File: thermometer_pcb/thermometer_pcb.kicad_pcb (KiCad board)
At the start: 2 copper layers, 76.6 x 49 mm, 23 parts, among them J1 POWER_IN, J2 TC_IN, J3 EXT_DS1, J4 EXT_DS2, J5 DISP, J6 Conn_01x02, J7 SPI, J8 I2C, J9 ENC, Q1 PN2222A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

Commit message: thermometer_pcb: move to new kicad
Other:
- net class Default removed
- net class PWR removed
- net class tc removed

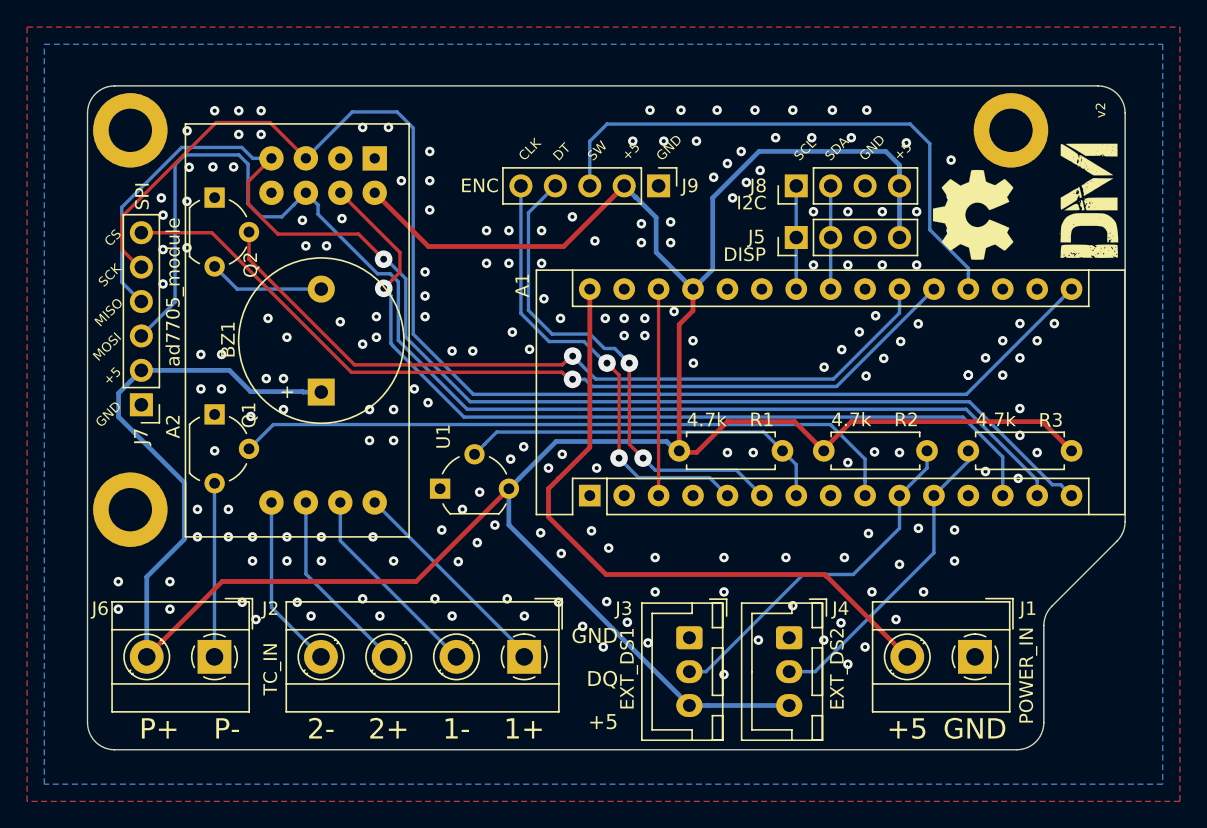
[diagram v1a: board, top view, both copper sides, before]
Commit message: pcb: tune corners radius
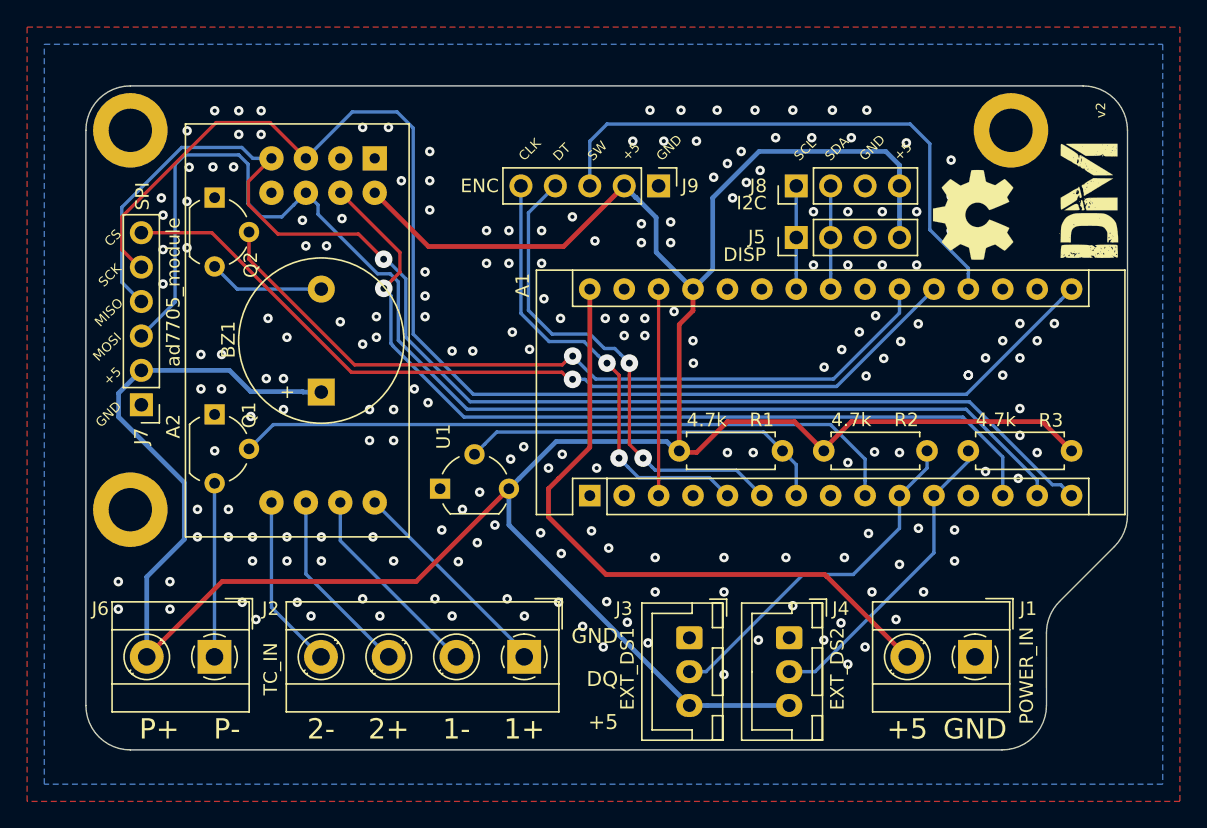
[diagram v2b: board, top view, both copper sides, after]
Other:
- board size 76.6 x 49 mm -> 76.9 x 49 mm
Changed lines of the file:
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@@
   (setup
     (aux_axis_origin 139.446 106.807)
-    (grid_origin 222.205677 44.032604)
+    (grid_origin 148.796676 47.298604)
     (pcbplotparams
       (layerselection 0x030f0_ffffffff)
@@
       (net 1 "GND") (zone_connect 2))
   )
+  (gr_arc (start 219.695641 84.398259) (end 216.415641 84.398259) (angle 45.00852154) (layer "Edge.Cuts") (width 0.1))
+  (gr_arc (start 219.116676 75.698604) (end 222.396676 75.698604) (angle 45) (layer "Edge.Cuts") (width 0.1))
+  (gr_arc (start 219.116676 47.298604) (end 222.396676 47.298604) (angle -90) (layer "Edge.Cuts") (width 0.1))
+  (gr_arc (start 213.136676 89.748604) (end 213.136676 93.028604) (angle -90) (layer "Edge.Cuts") (width 0.1))
+  (gr_arc (start 148.796676 89.748604) (end 145.516676 89.748604) (angle -90) (layer "Edge.Cuts") (width 0.1))
+  (gr_arc (start 148.796676 47.298604) (end 148.796676 44.018604) (angle -90) (layer "Edge.Cuts") (width 0.1))
   (gr_text "v2" (at 220.427677 45.810604 90) (layer "F.SilkS")
     (effects (font (size 0.7 0.7) (thickness 0.1)))
@@
   (gr_circle (center 218.268677 59.018604) (end 218.268677 58.618605) (layer "Dwgs.User") (width 0.1))
   (gr_circle (center 218.268677 74.258604) (end 218.268677 73.858604) (layer "Dwgs.User") (width 0.1))
-  (gr_line (start 145.636676 46.018604) (end 145.636676 91.018604) (layer "Edge.Cuts") (width 0.1))
-  (gr_line (start 216.807463 82.432818) (end 221.63589 77.604391) (layer "Edge.Cuts") (width 0.1))
-  (gr_arc (start 218.221676 83.847031) (end 216.807463 82.432818) (angle -45) (layer "Edge.Cuts") (width 0.1))
-  (gr_line (start 220.221676 44.018604) (end 147.636676 44.018604) (layer "Edge.Cuts") (width 0.1))
-  (gr_arc (start 147.636676 46.018604) (end 147.636676 44.018604) (angle -90) (layer "Edge.Cuts") (width 0.1))
-  (gr_arc (start 147.636676 91.018604) (end 145.636676 91.018604) (angle -90) (layer "Edge.Cuts") (width 0.1))
-  (gr_line (start 147.636676 93.018604) (end 214.221676 93.018604) (layer "Edge.Cuts") (width 0.1))
-  (gr_arc (start 214.221676 91.018604) (end 214.221676 93.018604) (angle -90) (layer "Edge.Cuts") (width 0.1))
-  (gr_line (start 216.221676 91.018604) (end 216.221676 83.847031) (layer "Edge.Cuts") (width 0.1))
-  (gr_arc (start 220.221676 76.190177) (end 221.63589 77.604391) (angle -45) (layer "Edge.Cuts") (width 0.1))
-  (gr_line (start 222.221676 76.190177) (end 222.221676 46.018604) (layer "Edge.Cuts") (width 0.1))
-  (gr_arc (start 220.221676 46.018604) (end 222.221676 46.018604) (angle -90) (layer "Edge.Cuts") (width 0.1))
+  (gr_line (start 145.516676 47.298604) (end 145.516676 89.748604) (layer "Edge.Cuts") (width 0.1))
+  (gr_line (start 217.376676 82.078604) (end 221.435986 78.017914) (layer "Edge.Cuts") (width 0.1))
+  (gr_line (start 219.116676 44.018604) (end 148.796676 44.018604) (layer "Edge.Cuts") (width 0.1))
+  (gr_line (start 148.796676 93.028604) (end 213.136676 93.028604) (layer "Edge.Cuts") (width 0.1))
+  (gr_line (start 216.416676 89.748604) (end 216.415641 84.398259) (layer "Edge.Cuts") (width 0.1))
+  (gr_line (start 222.396676 75.698604) (end 222.396676 47.298604) (layer "Edge.Cuts") (width 0.1))
   (segment (start 202.155677 80.082604) (end 205.568677 76.669604) (width 0.25) (layer "B.Cu") (net 20))
   (segment (start 205.568677 76.669604) (end 205.568677 74.258604) (width 0.25) (layer "B.Cu") (net 20))

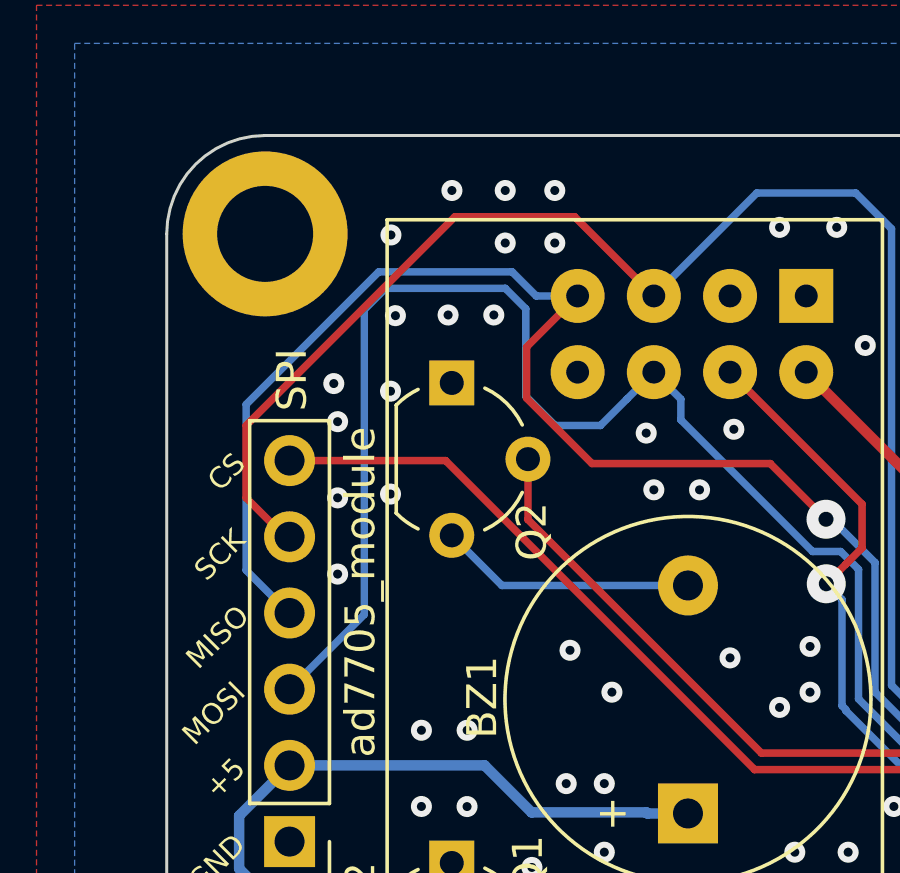
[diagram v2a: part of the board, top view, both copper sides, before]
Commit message: pcb: move some traces
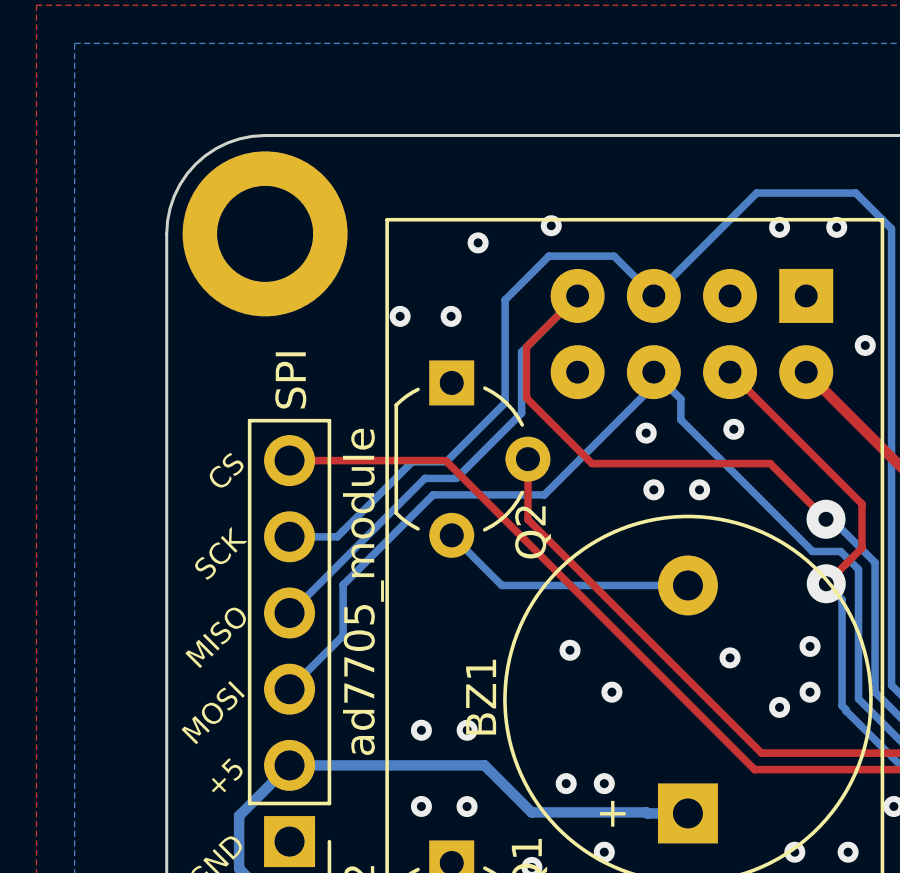
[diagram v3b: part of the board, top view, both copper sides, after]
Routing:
- net /11(**/MOSI): track 95.1 -> 84.9 mm
- net /12(MISO): track 97.1 -> 91.5 mm
- net /13(SCK): track 100.7 -> 97.3 mm
- net GND: vias 201 -> 190
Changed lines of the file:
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@@
     (thickness 1.6)
     (drawings 76)
-    (tracks 437)
+    (tracks 424)
     (modules 23)
     (nets 26)
@@
   (gr_line (start 216.416676 89.748604) (end 216.415641 84.398259) (layer "Edge.Cuts") (width 0.1))
   (gr_line (start 222.396676 75.698604) (end 222.396676 47.298604) (layer "Edge.Cuts") (width 0.1))
+  (via micro (at 155.896676 47.598604) (size 0.7) (drill 0.3) (layers "F.Cu" "B.Cu") (net 1))
+  (segment (start 149.611177 57.395104) (end 151.200176 57.395104) (width 0.25) (layer "B.Cu") (net 3))
+  (segment (start 151.200176 57.395104) (end 151.396676 57.198604) (width 0.25) (layer "B.Cu") (net 3))
+  (segment (start 156.796676 49.498604) (end 158.253677 48.041603) (width 0.25) (layer "B.Cu") (net 3))
+  (segment (start 156.796676 52.932727) (end 156.796676 49.498604) (width 0.25) (layer "B.Cu") (net 3))
+  (segment (start 154.830821 54.898582) (end 156.796676 52.932727) (width 0.25) (layer "B.Cu") (net 3))
+  (segment (start 151.396676 57.198604) (end 153.696698 54.898582) (width 0.25) (layer "B.Cu") (net 3))
+  (segment (start 153.696698 54.898582) (end 154.830821 54.898582) (width 0.25) (layer "B.Cu") (net 3))
+  (segment (start 158.253677 48.041603) (end 160.428676 48.041603) (width 0.25) (layer "B.Cu") (net 3))
+  (segment (start 160.428676 48.041603) (end 161.753677 49.366604) (width 0.25) (layer "B.Cu") (net 3))
+  (via micro (at 154.996676 50.048604) (size 0.7) (drill 0.3) (layers "F.Cu" "B.Cu") (net 1))
+  (segment (start 154.12452 55.448593) (end 155.168855 55.448593) (width 0.25) (layer "B.Cu") (net 4))
+  (segment (start 157.346687 51.233594) (end 159.213677 49.366604) (width 0.25) (layer "B.Cu") (net 4))
+  (segment (start 149.638009 59.935104) (end 154.12452 55.448593) (width 0.25) (layer "B.Cu") (net 4))
+  (segment (start 149.611177 59.935104) (end 149.638009 59.935104) (width 0.25) (layer "B.Cu") (net 4))
+  (segment (start 157.346687 53.270761) (end 157.346687 51.233594) (width 0.25) (layer "B.Cu") (net 4))
+  (segment (start 155.168855 55.448593) (end 157.346687 53.270761) (width 0.25) (layer "B.Cu") (net 4))
+  (segment (start 158.104799 55.998604) (end 161.753677 52.349726) (width 0.25) (layer "B.Cu") (net 6))
+  (segment (start 151.396676 60.689605) (end 151.396676 58.998604) (width 0.25) (layer "B.Cu") (net 6))
+  (segment (start 161.753677 52.349726) (end 161.753677 51.906604) (width 0.25) (layer "B.Cu") (net 6))
+  (segment (start 149.611177 62.475104) (end 151.396676 60.689605) (width 0.25) (layer "B.Cu") (net 6))
+  (segment (start 154.396676 55.998604) (end 158.104799 55.998604) (width 0.25) (layer "B.Cu") (net 6))
+  (segment (start 151.396676 58.998604) (end 154.396676 55.998604) (width 0.25) (layer "B.Cu") (net 6))
+  (via micro (at 158.335628 47.025726) (size 0.7) (drill 0.3) (layers "F.Cu" "B.Cu") (net 1))
+  (via micro (at 153.296676 50.048604) (size 0.7) (drill 0.3) (layers "F.Cu" "B.Cu") (net 1))
   (segment (start 202.155677 80.082604) (end 205.568677 76.669604) (width 0.25) (layer "B.Cu") (net 20))
   (segment (start 205.568677 76.669604) (end 205.568677 74.258604) (width 0.25) (layer "B.Cu") (net 20))
@@
   (via micro (at 209.378677 49.493604) (size 0.7) (drill 0.3) (layers "F.Cu" "B.Cu") (net 1))
   (via micro (at 165.944677 47.080604) (size 0.7) (drill 0.3) (layers "F.Cu" "B.Cu") (net 1))
-  (via micro (at 154.895677 50.001604) (size 0.7) (drill 0.3) (layers "F.Cu" "B.Cu") (net 1))
-  (via micro (at 156.419677 50.001604) (size 0.7) (drill 0.3) (layers "F.Cu" "B.Cu") (net 1))
   (via micro (at 170.897677 48.858604) (size 0.7) (drill 0.3) (layers "F.Cu" "B.Cu") (net 1))
   (via micro (at 170.897677 51.017604) (size 0.7) (drill 0.3) (layers "F.Cu" "B.Cu") (net 1))
@@
   (via micro (at 153.752677 77.306604) (size 0.7) (drill 0.3) (layers "F.Cu" "B.Cu") (net 1))
   (via micro (at 153.752677 75.274604) (size 0.7) (drill 0.3) (layers "F.Cu" "B.Cu") (net 1))
-  (via micro (at 156.800677 47.602114) (size 0.7) (drill 0.3) (layers "F.Cu" "B.Cu") (net 1))
-  (via micro (at 155.022677 45.852094) (size 0.7) (drill 0.3) (layers "F.Cu" "B.Cu") (net 1))
-  (via micro (at 158.451677 47.602114) (size 0.7) (drill 0.3) (layers "F.Cu" "B.Cu") (net 1))
-  (via micro (at 156.800677 45.852094) (size 0.7) (drill 0.3) (layers "F.Cu" "B.Cu") (net 1))
-  (via micro (at 158.451677 45.852094) (size 0.7) (drill 0.3) (layers "F.Cu" "B.Cu") (net 1))
-  (segment (start 160.853678 52.806603) (end 161.753677 51.906604) (width 0.25) (layer "B.Cu") (net 6))
-  (segment (start 152.101677 59.984604) (end 152.101677 49.824604) (width 0.25) (layer "B.Cu") (net 6))
-  (via micro (at 153.139903 50.02383) (size 0.7) (drill 0.3) (layers "F.Cu" "B.Cu") (net 1))
-  (segment (start 152.101677 49.824604) (end 152.813677 49.112604) (width 0.25) (layer "B.Cu") (net 6))
-  (via micro (at 152.976687 52.541604) (size 0.7) (drill 0.3) (layers "F.Cu" "B.Cu") (net 1))
-  (via micro (at 152.976687 55.970604) (size 0.7) (drill 0.3) (layers "F.Cu" "B.Cu") (net 1))
-  (segment (start 149.611177 62.475104) (end 152.101677 59.984604) (width 0.25) (layer "B.Cu") (net 6))
-  (segment (start 152.813677 49.112604) (end 156.800677 49.112604) (width 0.25) (layer "B.Cu") (net 6))
-  (segment (start 156.800677 49.112604) (end 157.485177 49.797104) (width 0.25) (layer "B.Cu") (net 6))
-  (segment (start 157.485177 49.797104) (end 157.485177 52.707104) (width 0.25) (layer "B.Cu") (net 6))
-  (segment (start 157.485177 52.707104) (end 158.462677 53.684604) (width 0.25) (layer "B.Cu") (net 6))
-  (segment (start 159.975677 53.684604) (end 160.853678 52.806603) (width 0.25) (layer "B.Cu") (net 6))
-  (segment (start 158.462677 53.684604) (end 159.975677 53.684604) (width 0.25) (layer "B.Cu") (net 6))
-  (via micro (at 151.212677 58.637604) (size 0.7) (drill 0.3) (layers "F.Cu" "B.Cu") (net 1))
-  (via micro (at 151.212677 56.097604) (size 0.7) (drill 0.3) (layers "F.Cu" "B.Cu") (net 1))
-  (via micro (at 151.212677 53.557604) (size 0.7) (drill 0.3) (layers "F.Cu" "B.Cu") (net 1))
   (via micro (at 163.277677 55.829614) (size 0.7) (drill 0.3) (layers "F.Cu" "B.Cu") (net 1))
   (via micro (at 164.420677 53.811604) (size 0.7) (drill 0.3) (layers "F.Cu" "B.Cu") (net 1))
@@
   (via micro (at 167.849677 47.080604) (size 0.7) (drill 0.3) (layers "F.Cu" "B.Cu") (net 1))
   (via micro (at 170.552187 61.050604) (size 0.7) (drill 0.3) (layers "F.Cu" "B.Cu") (net 1))
-  (segment (start 157.832507 49.366604) (end 159.213677 49.366604) (width 0.25) (layer "B.Cu") (net 4))
-  (segment (start 149.589177 59.935104) (end 148.164677 58.510604) (width 0.25) (layer "B.Cu") (net 4))
-  (segment (start 149.611177 59.935104) (end 149.589177 59.935104) (width 0.25) (layer "B.Cu") (net 4))
-  (segment (start 157.028498 48.562594) (end 157.832507 49.366604) (width 0.25) (layer "B.Cu") (net 4))
-  (segment (start 148.164677 58.510604) (end 148.164677 52.983773) (width 0.25) (layer "B.Cu") (net 4))
-  (segment (start 148.164677 52.983773) (end 152.585856 48.562594) (width 0.25) (layer "B.Cu") (net 4))
-  (segment (start 152.585856 48.562594) (end 157.028498 48.562594) (width 0.25) (layer "B.Cu") (net 4))
   (via (at 185.629677 64.479604) (size 1.3) (drill 0.5) (layers "F.Cu" "B.Cu") (net 21))
   (segment (start 185.629721 65.398842) (end 185.629721 64.479604) (width 0.25) (layer "F.Cu") (net 21))
@@
   (segment (start 182.727708 62.339635) (end 183.788155 63.400082) (width 0.25) (layer "B.Cu") (net 21))
   (segment (start 179.933705 62.339635) (end 182.727708 62.339635) (width 0.25) (layer "B.Cu") (net 21))
-  (segment (start 149.462177 57.395104) (end 149.611177 57.395104) (width 0.25) (layer "F.Cu") (net 3))
-  (segment (start 148.164677 56.097604) (end 149.462177 57.395104) (width 0.25) (layer "F.Cu") (net 3))
-  (via micro (at 152.990677 47.334604) (size 0.7) (drill 0.3) (layers "F.Cu" "B.Cu") (net 1))
-  (segment (start 148.164677 53.684604) (end 148.164677 56.097604) (width 0.25) (layer "F.Cu") (net 3))
-  (via micro (at 151.085677 52.287604) (size 0.7) (drill 0.3) (layers "F.Cu" "B.Cu") (net 1))
-  (segment (start 161.753677 49.366604) (end 159.114177 46.727104) (width 0.25) (layer "F.Cu") (net 3))
-  (segment (start 159.114177 46.727104) (end 155.122177 46.727104) (width 0.25) (layer "F.Cu") (net 3))
-  (segment (start 155.122177 46.727104) (end 148.164677 53.684604) (width 0.25) (layer "F.Cu") (net 3))
   (via micro (at 200.005677 64.779974) (size 0.7) (drill 0.3) (layers "F.Cu" "B.Cu") (net 1))
   (via micro (at 190.355677 64.482604) (size 0.7) (drill 0.3) (layers "F.Cu" "B.Cu") (net 1))
